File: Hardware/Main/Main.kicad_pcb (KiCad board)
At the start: 4 copper layers, 19 parts, among them J1 POWERBOARD, SW3 SW_Push, SW4 RotaryEncoder_Switch, SW5 SW_Push, U1 TFT_ST7789, U2 ESP32-WROOM-32D

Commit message: Library paths relative instead of absolute
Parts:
- renumbered RST to SW1, PROG to SW2
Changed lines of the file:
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@@
     (property "ki_keywords" "switch normally-open pushbutton push-button")
     (attr smd)
-    (fp_text reference "RST" (at 0 3.2 90) (layer "B.SilkS")
+    (fp_text reference "SW1" (at 0 3.2 90) (layer "B.SilkS")
         (effects (font (size 1 1) (thickness 0.15)) (justify mirror))
     )
@@
     (property "ki_keywords" "switch normally-open pushbutton push-button")
     (attr smd)
-    (fp_text reference "PROG" (at 0 3.2 90) (layer "B.SilkS")
-        (effects (font (size 1 1) (thickness 0.15)) (justify mirror))
-    )
+    (fp_text reference "SW2" (at 0 3.2 90) (layer "B.SilkS")
+        (effects (font (size 1 1) (thickness 0.15)) (justify mirror))
+    )

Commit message: Mainboard edge cuts
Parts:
- SW1, SW2: moved to F.Cu
- moved SW2 133.3 mm to (69.3, 91.0), turned to 90 degrees
- moved SW1 128.8 mm to (69.3, 81.7), turned to 90 degrees
- moved D1 121.4 mm to (69.6, 60.8)
- moved D2 121.4 mm to (105.1, 60.8)
- moved H1 121.4 mm to (98.8, 55.6)
- moved H2 121.4 mm to (75.9, 55.6)
- moved H3 121.4 mm to (103.4, 55.6)
- moved H4 121.4 mm to (71.4, 55.6)
- moved H5 121.4 mm to (103.4, 113.5)
- moved J1 121.4 mm to (87.4, 84.9)
- moved Per1 121.4 mm to (87.4, 117.3)
- moved Per2 121.4 mm to (105.1, 73.5)
- moved Per3 121.4 mm to (69.6, 73.5)
- moved SW3 121.4 mm to (70.1, 104.4)
- moved SW4 121.4 mm to (89.9, 99.2)
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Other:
- board outline added: 43.4 x 70.9 mm

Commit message: Mainboard routing etc
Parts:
- added C1: C, Capacitor_SMD:C_0805_2012Metric_Pad1.18x1.45mm_HandSolder, B.Cu at (-6.86, -21.1)
- added C2: 0.1uF, Capacitor_SMD:C_0805_2012Metric_Pad1.18x1.45mm_HandSolder, B.Cu at (-6.86, -24.9)
- added C3: 0.1uF, Capacitor_SMD:C_0805_2012Metric_Pad1.18x1.45mm_HandSolder, B.Cu at (-17.8, -24.1)
- added C4: 0.1uF, Capacitor_SMD:C_0805_2012Metric_Pad1.18x1.45mm_HandSolder, B.Cu at (17.8, -24.1)
- added C5: 22uF, Capacitor_SMD:CP_Elec_4x5.3, F.Cu at (-12.4, -19.0)
- added C6: 0.1uF, Capacitor_SMD:C_0805_2012Metric_Pad1.18x1.45mm_HandSolder, F.Cu at (13.3, -3.81)
- added C7: 0.1uF, Capacitor_SMD:C_0805_2012Metric_Pad1.18x1.45mm_HandSolder, F.Cu at (6.35, 8.13)
- added R1: 10K, Resistor_SMD:R_0805_2012Metric_Pad1.20x1.40mm_HandSolder, B.Cu at (-4.83, -21.1)
- added R10: 10K, Resistor_SMD:R_0805_2012Metric_Pad1.20x1.40mm_HandSolder, F.Cu at (13.4, -5.84)
- added R11: 10K, Resistor_SMD:R_0805_2012Metric_Pad1.20x1.40mm_HandSolder, F.Cu at (17.2, -5.84)
- added R12: 10K, Resistor_SMD:R_0805_2012Metric_Pad1.20x1.40mm_HandSolder, F.Cu at (16.9, 3.81)
- added R13: 10K, Resistor_SMD:R_0805_2012Metric_Pad1.20x1.40mm_HandSolder, F.Cu at (13.1, 3.81)
- added R14: 1K, Resistor_SMD:R_0805_2012Metric_Pad1.20x1.40mm_HandSolder, B.Cu at (1.02, 25.3)
- added R15: 1K, Resistor_SMD:R_0805_2012Metric_Pad1.20x1.40mm_HandSolder, F.Cu at (-11.7, 16.8)
- added R16: 1K, Resistor_SMD:R_0805_2012Metric_Pad1.20x1.40mm_HandSolder, B.Cu at (2.41, 17.4)
- added R17: 10K, Resistor_SMD:R_0805_2012Metric_Pad1.20x1.40mm_HandSolder, F.Cu at (11.7, 16.8)
- added R18: 1K, Resistor_SMD:R_0805_2012Metric_Pad1.20x1.40mm_HandSolder, B.Cu at (-2.41, 17.4)
- added R19: 10K, Resistor_SMD:R_0805_2012Metric_Pad1.20x1.40mm_HandSolder, F.Cu at (13.1, 5.84)
- added R2: 10K, Resistor_SMD:R_0805_2012Metric_Pad1.20x1.40mm_HandSolder, B.Cu at (6.99, -10.6)
- added R20: 1K, Resistor_SMD:R_0805_2012Metric_Pad1.20x1.40mm_HandSolder, F.Cu at (16.2, 16.8)
- added R21: 1K, Resistor_SMD:R_0805_2012Metric_Pad1.20x1.40mm_HandSolder, B.Cu at (-15.7, -24.1)
- added R3: 100K, Resistor_SMD:R_0805_2012Metric_Pad1.20x1.40mm_HandSolder, F.Cu at (-1.00, 3.30)
- added R4: 100K, Resistor_SMD:R_0805_2012Metric_Pad1.20x1.40mm_HandSolder, F.Cu at (-4.81, 3.30)
- added R5: 10K, Resistor_SMD:R_0805_2012Metric_Pad1.20x1.40mm_HandSolder, F.Cu at (17.1, -3.81)
- added R6: 10K, Resistor_SMD:R_0805_2012Metric_Pad1.20x1.40mm_HandSolder, B.Cu at (-4.45, 17.4)
- added R7: 10K, Resistor_SMD:R_0805_2012Metric_Pad1.20x1.40mm_HandSolder, B.Cu at (4.45, 17.4)
- added R8: 10K, Resistor_SMD:R_0805_2012Metric_Pad1.20x1.40mm_HandSolder, B.Cu at (-1.02, 25.3)
- added R9: 10K, Resistor_SMD:R_0805_2012Metric_Pad1.20x1.40mm_HandSolder, F.Cu at (-16.2, 16.8)
- added U3: TCA4311a, Package_SO:SOIC-8_3.9x4.9mm_P1.27mm, F.Cu at (15.1, 0.00)
- moved D1 121.8 mm to (-17.8, -24.1)
- moved D2 121.8 mm to (17.8, -24.1)
- moved H3 121.8 mm to (16.0, -29.3)
- moved H5 121.8 mm to (16.0, 28.6)
- moved J1 121.8 mm to (0.00, 0.00)
- moved Per1 121.8 mm to (0.00, 32.4)
- moved Per2 121.8 mm to (17.8, -11.4)
- moved Per3 121.8 mm to (-17.8, -11.4)
- moved SW3 121.8 mm to (-17.2, 19.5)
- moved SW4 121.8 mm to (2.50, 14.2)
- moved SW5 121.8 mm to (10.7, 19.5)
- moved U1 121.8 mm to (0.00, 10.5)
- moved U2 121.8 mm to (0.00, -17.8)
- moved H1 121.8 mm to (11.4, -29.3)
- moved H2 121.8 mm to (-11.4, -29.3)
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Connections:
- U2 pad 4: BatSense -> ChargeState
- U2 pad 5: ChargeState -> BatSense
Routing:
- net GND: track 0.00 -> 261.5 mm, vias 0 -> 15
- net +3.3VP: track 0.00 -> 144.9 mm, vias 0 -> 4
- net +3.3V: track 0.00 -> 134.4 mm, vias 0 -> 10
- net SDA_PER: track 0.00 -> 130.2 mm, vias 0 -> 3
- net SCL_PER: track 0.00 -> 112.0 mm, vias 0 -> 1
- net +BATT: track 0.00 -> 97.3 mm, vias 0 -> 3
- net RESET: track 0.00 -> 60.6 mm, vias 0 -> 1
- net ID0Prog: track 0.00 -> 52.9 mm, vias 0 -> 2
- net Net-(D1-DOUT): track 0.00 -> 43.4 mm
- net ChargeState: track 0.00 -> 32.9 mm
- net TX: track 0.00 -> 32.0 mm, vias 0 -> 1
- net BatSense: track 0.00 -> 28.7 mm
- net RX: track 0.00 -> 27.0 mm, vias 0 -> 1
- net Net-(R17-Pad1): track 0.00 -> 11.9 mm
- net Net-(R15-Pad1): track 0.00 -> 11.9 mm
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- added copper zone on In1.Cu, net GND

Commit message: Progress with main board
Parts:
- added J2: ProgHeader, Connectors:ESP32ProgHeader, F.Cu at (18.2, 9.27)
- added R22: 1K, Resistor_SMD:R_0805_2012Metric_Pad1.20x1.40mm_HandSolder, B.Cu at (2.54, 7.60)
- added R23: 1K, Resistor_SMD:R_0805_2012Metric_Pad1.20x1.40mm_HandSolder, B.Cu at (0.00, 7.60)
- added R24: 1K, Resistor_SMD:R_0805_2012Metric_Pad1.20x1.40mm_HandSolder, B.Cu at (-2.54, 7.60)
- added R25: 1K, Resistor_SMD:R_0805_2012Metric_Pad1.20x1.40mm_HandSolder, B.Cu at (-5.08, 7.60)
- added R26: 1K, Resistor_SMD:R_0805_2012Metric_Pad1.20x1.40mm_HandSolder, B.Cu at (-7.62, 7.60)
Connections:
- U1 pad 3: unconnected-(U1-SCK-Pad3) -> Net-(U1-SCK)
- U1 pad 4: unconnected-(U1-SDA-Pad4) -> Net-(U1-SDA)
- U1 pad 5: unconnected-(U1-RES-Pad5) -> Net-(U1-RES)
- U1 pad 6: unconnected-(U1-DC-Pad6) -> Net-(U1-DC)
- U1 pad 7: unconnected-(U1-BLK-Pad7) -> Net-(U1-BLK)
- U2 pad 10: unconnected-(U2-IO25-Pad10) -> ButtonA
- U2 pad 11: unconnected-(U2-IO26-Pad11) -> RotaryButton
- U2 pad 12: unconnected-(U2-IO27-Pad12) -> RotaryA
- U2 pad 13: unconnected-(U2-IO14-Pad13) -> RotaryB
- U2 pad 14: unconnected-(U2-IO12-Pad14) -> ButtonB
- U2 pad 17: unconnected-(U2-SHD/SD2-Pad17) -> TFT_BLK
- U2 pad 18: unconnected-(U2-SWP/SD3-Pad18) -> TFT_DC
- U2 pad 19: unconnected-(U2-SCS/CMD-Pad19) -> TFT_RES
- U2 pad 20: unconnected-(U2-SCK/CLK-Pad20) -> TFT_SCK
- U2 pad 21: unconnected-(U2-SDO/SD0-Pad21) -> TFT_SDA
- U2 pad 6: unconnected-(U2-IO34-Pad6) -> WS2812Led
- U2 pad 8: unconnected-(U2-IO32-Pad8) -> SCL_ESP
- U2 pad 9: unconnected-(U2-IO33-Pad9) -> SDA_ESP
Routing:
- net RotaryA: track 0.00 -> 59.9 mm, vias 0 -> 1
- net RotaryButton: track 0.00 -> 59.4 mm, vias 0 -> 1
- net ButtonB: track 0.00 -> 55.4 mm, vias 0 -> 2
- net RotaryB: track 0.00 -> 53.6 mm, vias 0 -> 1
- net ButtonA: track 0.00 -> 37.3 mm, vias 0 -> 2
- net TFT_SCK: track 0.00 -> 36.2 mm, vias 0 -> 1
- net TFT_SDA: track 0.00 -> 35.7 mm, vias 0 -> 1
- net SDA_ESP: track 9.58 -> 45.0 mm, vias 0 -> 2
- net SCL_ESP: track 8.98 -> 42.1 mm, vias 0 -> 4
- net TFT_RES: track 0.00 -> 31.3 mm, vias 0 -> 1
- net TFT_DC: track 0.00 -> 28.4 mm, vias 0 -> 1
- net TFT_BLK: track 0.00 -> 25.0 mm, vias 0 -> 1
- net RX: track 27.0 -> 50.2 mm, vias 1 -> 2
- net ID0Prog: track 52.9 -> 75.8 mm
- net TX: track 32.0 -> 51.6 mm, vias 1 -> 2
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- added copper zone on B.Cu, net GND
- added copper zone on F.Cu, net GND
- added copper zone on In2.Cu, net GND

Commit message: Mainboard r0.1
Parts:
- moved C7 0.38 mm to (6.35, 7.75)
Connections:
- H1 pad 1: GND -> unconnected-(H1-Pad1)
- H2 pad 1: GND -> unconnected-(H2-Pad1)
- H3 pad 1: GND -> unconnected-(H3-Pad1)
- H4 pad 1: GND -> unconnected-(H4-Pad1)
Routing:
- net GND: track 266.9 -> 263.5 mm
- net RESET: track 77.4 -> 75.4 mm
- net SDA_PER: track 133.8 -> 132.9 mm
- net SCL_PER: track 118.9 -> 118.2 mm
- net +BATT: track 95.0 -> 94.5 mm
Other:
- board text added: "3.3V"
- board text added: "BAT"
- board text added: "GND"
- board text added: "Opencontroller Mainboard r0.1 (2024-09-15) https://github.com/eightonegulf/openController/"
- board text added: "PROG"
- board text added: "RESET"
- board text added: "SCL"
- board text added: "SDA"

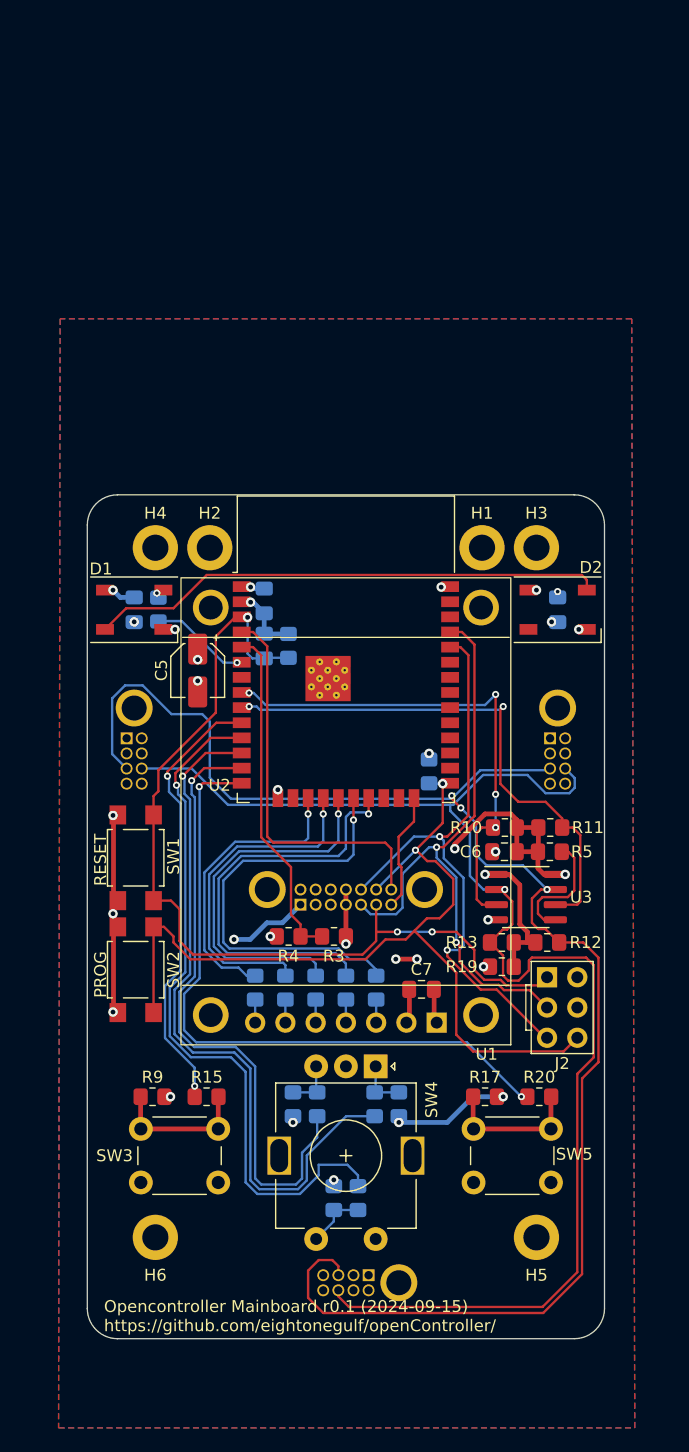
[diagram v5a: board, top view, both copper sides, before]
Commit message: Need to make more commits; Changed design to use horizontal peripheral connectors. Changed models, more compact design. Still in progress
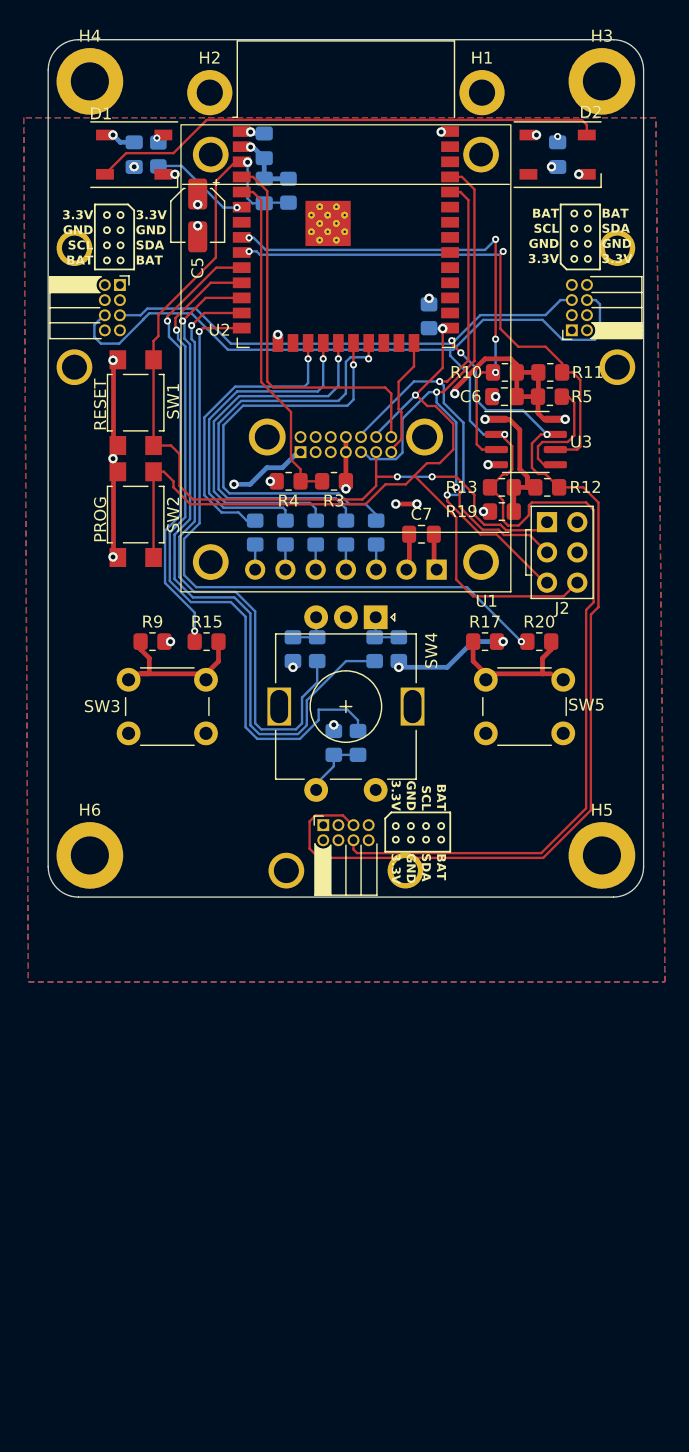
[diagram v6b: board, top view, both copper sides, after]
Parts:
- H3, H4, H5, H6: footprint MountingHole:MountingHole_2.2mm_M2_DIN965_Pad -> MountingHole:MountingHole_3.2mm_M3_DIN965_Pad
- Per1, Per2, Per3: moved to F.Cu
- moved H3 39.5 mm to (21.5, -68.5)
- moved H4 39.5 mm to (-21.5, -68.5)
- moved C2 38.2 mm to (-6.86, -63.1)
- moved C3 38.2 mm to (-17.8, -62.3)
- moved C4 38.2 mm to (17.8, -62.3)
- moved C5 38.2 mm to (-12.4, -57.2)
- moved C7 38.2 mm to (6.35, -30.5)
- moved H1 38.2 mm to (11.4, -67.6)
- moved H2 38.2 mm to (-11.4, -67.6)
- moved J2 38.2 mm to (18.2, -28.9)
- moved R1 38.2 mm to (-4.83, -59.3)
- moved R10 38.2 mm to (13.4, -44.1)
- moved R11 38.2 mm to (17.2, -44.1)
- moved R12 38.2 mm to (16.9, -34.4)
- moved R13 38.2 mm to (13.1, -34.4)
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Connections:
- Per1 pad 9: GND -> (no net)
- Per2 pad 9: GND -> (no net)
- Per3 pad 9: GND -> (no net)
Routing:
- net GND: track 263.5 -> 279.6 mm
- net +3.3VP: track 145.0 -> 156.9 mm
- net +BATT: track 94.5 -> 105.5 mm
- net SCL_PER: track 118.2 -> 128.3 mm
- net SDA_PER: track 132.9 -> 122.8 mm
- net Net-(R15-Pad1): track 11.9 -> 13.4 mm
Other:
- board size 43.4 x 70.9 mm -> 50 x 72 mm
- board text removed: "Opencontroller Mainboard r0.1 (2024-09-15) https://github.com/eightonegulf/openController/"

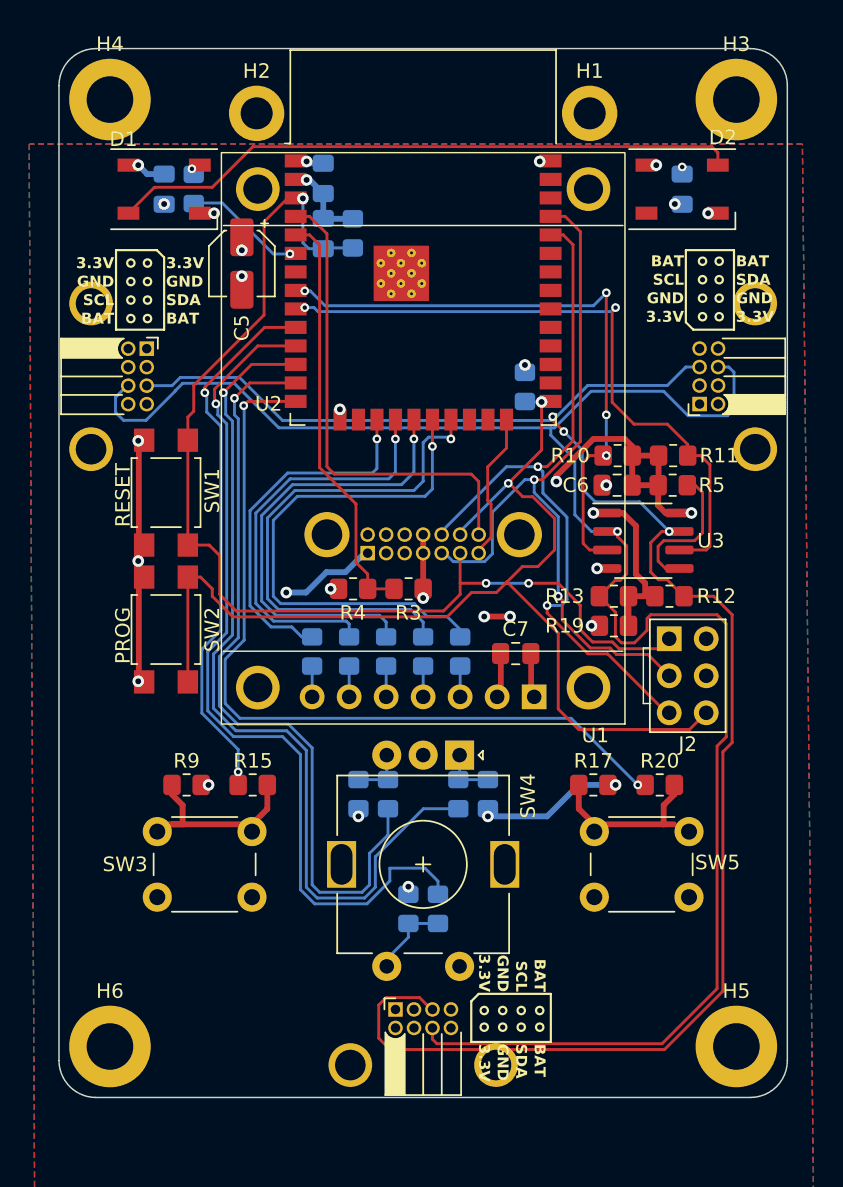
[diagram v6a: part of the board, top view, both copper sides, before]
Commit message: PCBBoard connector to other side of board
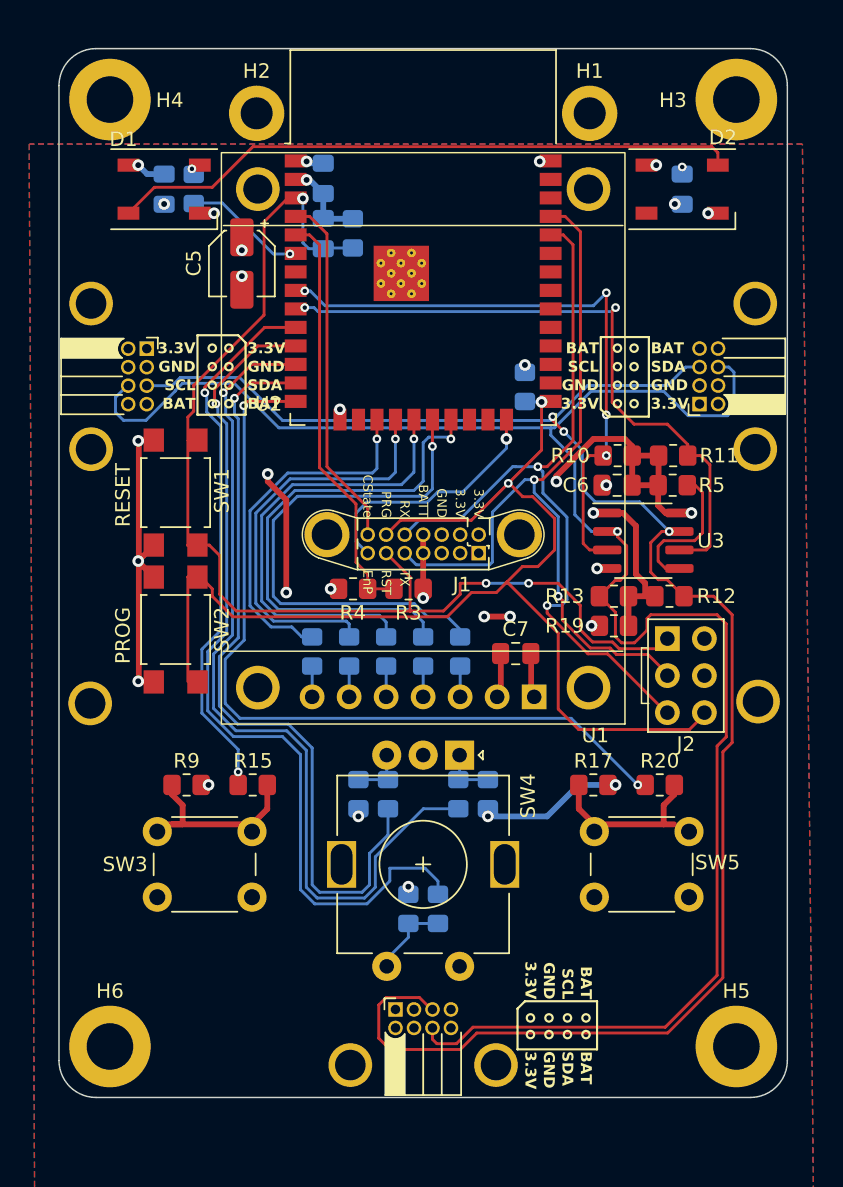
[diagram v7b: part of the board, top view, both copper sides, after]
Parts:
- added ?: , , F.Cu at (-22.9, -27.1)
- added ?: , , F.Cu at (23.0, -27.2)
- J1: moved to F.Cu
- moved SW1 0.66 mm to (-17.0, -41.5)
- moved SW2 0.66 mm to (-17.0, -32.1)
- moved J2 0.13 mm to (18.0, -29.0)
- turned J1 to 0 degrees
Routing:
- net GND: track 279.6 -> 324.6 mm
- net ChargeState: track 32.9 -> 24.4 mm
- net EnPower: track 9.93 -> 17.2 mm, vias 0 -> 1
- net ID0Prog: track 75.7 -> 80.9 mm
- net TX: track 51.2 -> 54.1 mm
- net +3.3V: track 143.3 -> 146.2 mm, vias 11 -> 12
- net RX: track 49.9 -> 52.5 mm
- net RESET: track 75.4 -> 77.8 mm
- net SCL_PER: track 128.3 -> 127.8 mm
- net SDA_PER: track 122.8 -> 122.3 mm
